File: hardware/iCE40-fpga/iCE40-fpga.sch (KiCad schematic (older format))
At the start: 45 parts, among them J1 USB_B_Micro, J2 JST_PH, J3 Feather, Q1 DMP2045U, U1 MCP73831-2-OT, U2 W25Q32JVZP, U3 AP2112K-3.3, U4 ICE40UP5K-SG48ITR, U5 NCV8114ASN120T1G, X1 DSC6101CI1A

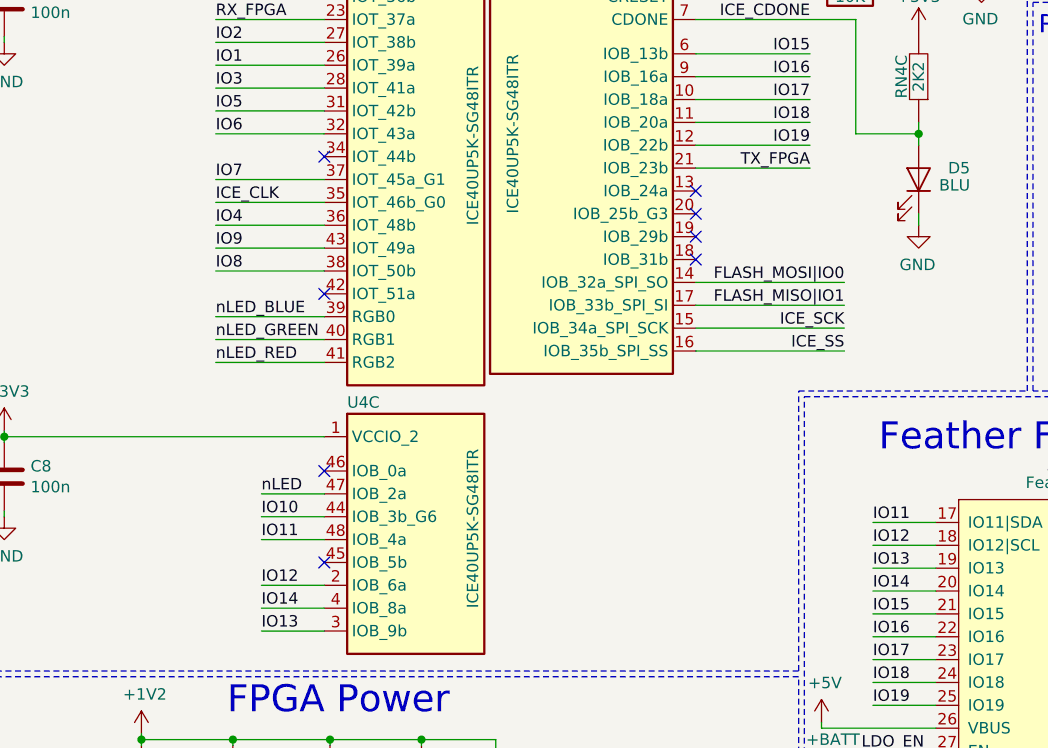
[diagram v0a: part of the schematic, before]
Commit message: broke out 4 pins to TP on bottom copper
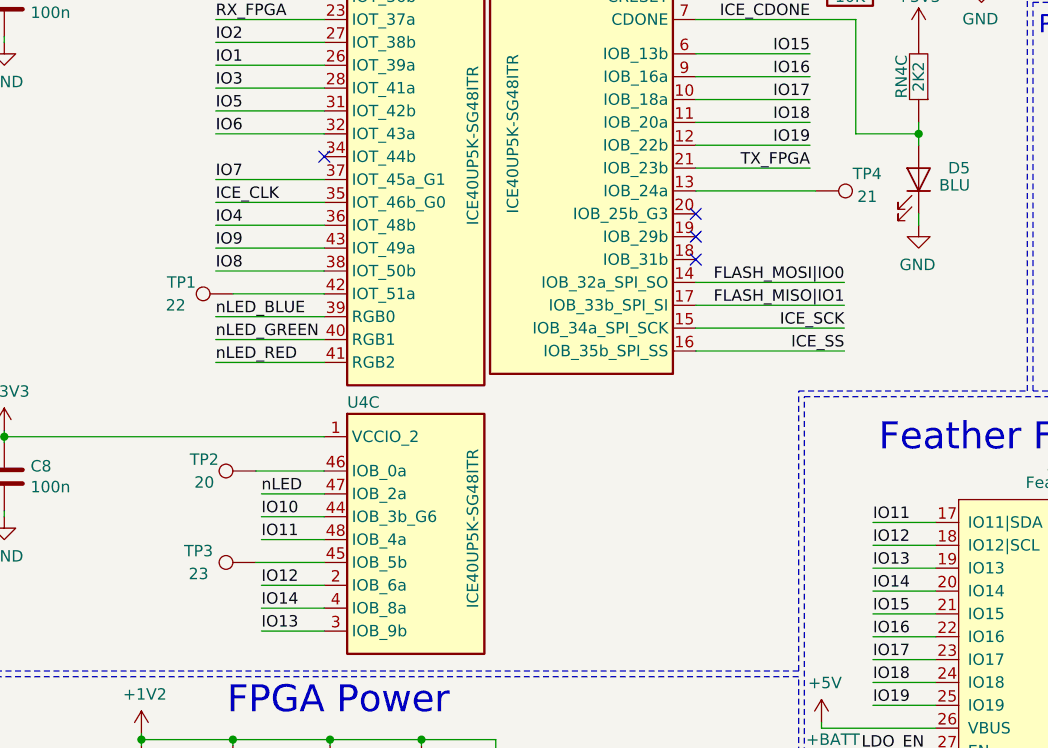
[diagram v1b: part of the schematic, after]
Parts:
- added TP1: 22, TestPoint:TestPoint_Pad_D1.5mm, symbol Connector:TestPoint
- added TP2: 20, TestPoint:TestPoint_Pad_D1.5mm, symbol Connector:TestPoint
- added TP3: 23, TestPoint:TestPoint_Pad_D1.5mm, symbol Connector:TestPoint
- added TP4: 21, TestPoint:TestPoint_Pad_D1.5mm, symbol Connector:TestPoint
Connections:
- net at U4.42 (IOT_51a): now also TP1.1
- net at U4.13 (IOB_24a): now also TP4.1
- net at U4.45 (IOB_5b): now also TP3.1
- net at U4.46 (IOB_0a): now also TP2.1
- no-connect marks 17 -> 13
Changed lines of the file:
@@
 	9875 5850 10000 5850
 NoConn ~ 6900 1900
-NoConn ~ 6900 2500
-NoConn ~ 8525 2350
 NoConn ~ 8525 2250
 NoConn ~ 8525 2150
-NoConn ~ 8525 2050
-NoConn ~ 6900 3275
+NoConn ~ 8525 2350
 Wire Wire Line
 	625  3100 975  3100
@@
 Wire Wire Line
 	10875 1975 10875 2025
-NoConn ~ 6900 3675
 Wire Wire Line
 	10700 1050 10725 1050
@@
 Wire Wire Line
 	4000 3300 4050 3300
+$Comp
+L Connector:TestPoint TP3
+U 1 1 5D23FA3D
+P 6600 3675
+F 0 "TP3" V 6650 3925 50  0000 C CNN
+F 1 "23" V 6550 3925 50  0000 C CNN
+F 2 "TestPoint:TestPoint_Pad_D1.5mm" H 6800 3675 50  0001 C CNN
+F 3 "~" H 6800 3675 50  0001 C CNN
+	1    6600 3675
+	0    -1   -1   0
+$EndComp
+Wire Wire Line
+	6600 3675 6900 3675
+$Comp
+L Connector:TestPoint TP2
+U 1 1 5D26AE62
+P 6600 3275
+F 0 "TP2" V 6650 3500 50  0000 C CNN
+F 1 "20" V 6550 3500 50  0000 C CNN
+F 2 "TestPoint:TestPoint_Pad_D1.5mm" H 6800 3275 50  0001 C CNN
+F 3 "~" H 6800 3275 50  0001 C CNN
+	1    6600 3275
+	0    -1   -1   0
+$EndComp
+Wire Wire Line
+	6600 3275 6900 3275
+$Comp
+L Connector:TestPoint TP1
+U 1 1 5D28130D
+P 6500 2500
+F 0 "TP1" V 6550 2725 50  0000 C CNN
+F 1 "22" V 6450 2750 50  0000 C CNN
+F 2 "TestPoint:TestPoint_Pad_D1.5mm" H 6700 2500 50  0001 C CNN
+F 3 "~" H 6700 2500 50  0001 C CNN
+	1    6500 2500
+	0    -1   -1   0
+$EndComp
+Wire Wire Line
+	6500 2500 6900 2500
+$Comp
+L Connector:TestPoint TP4
+U 1 1 5D2B0957
+P 9050 2050
+F 0 "TP4" V 8975 2275 50  0000 C CNN
+F 1 "21" V 9075 2275 50  0000 C CNN
+F 2 "TestPoint:TestPoint_Pad_D1.5mm" H 9250 2050 50  0001 C CNN
+F 3 "~" H 9250 2050 50  0001 C CNN
+	1    9050 2050
+	0    1    1    0
+$EndComp
+Wire Wire Line
+	9050 2050 8525 2050
 $EndSCHEMATC

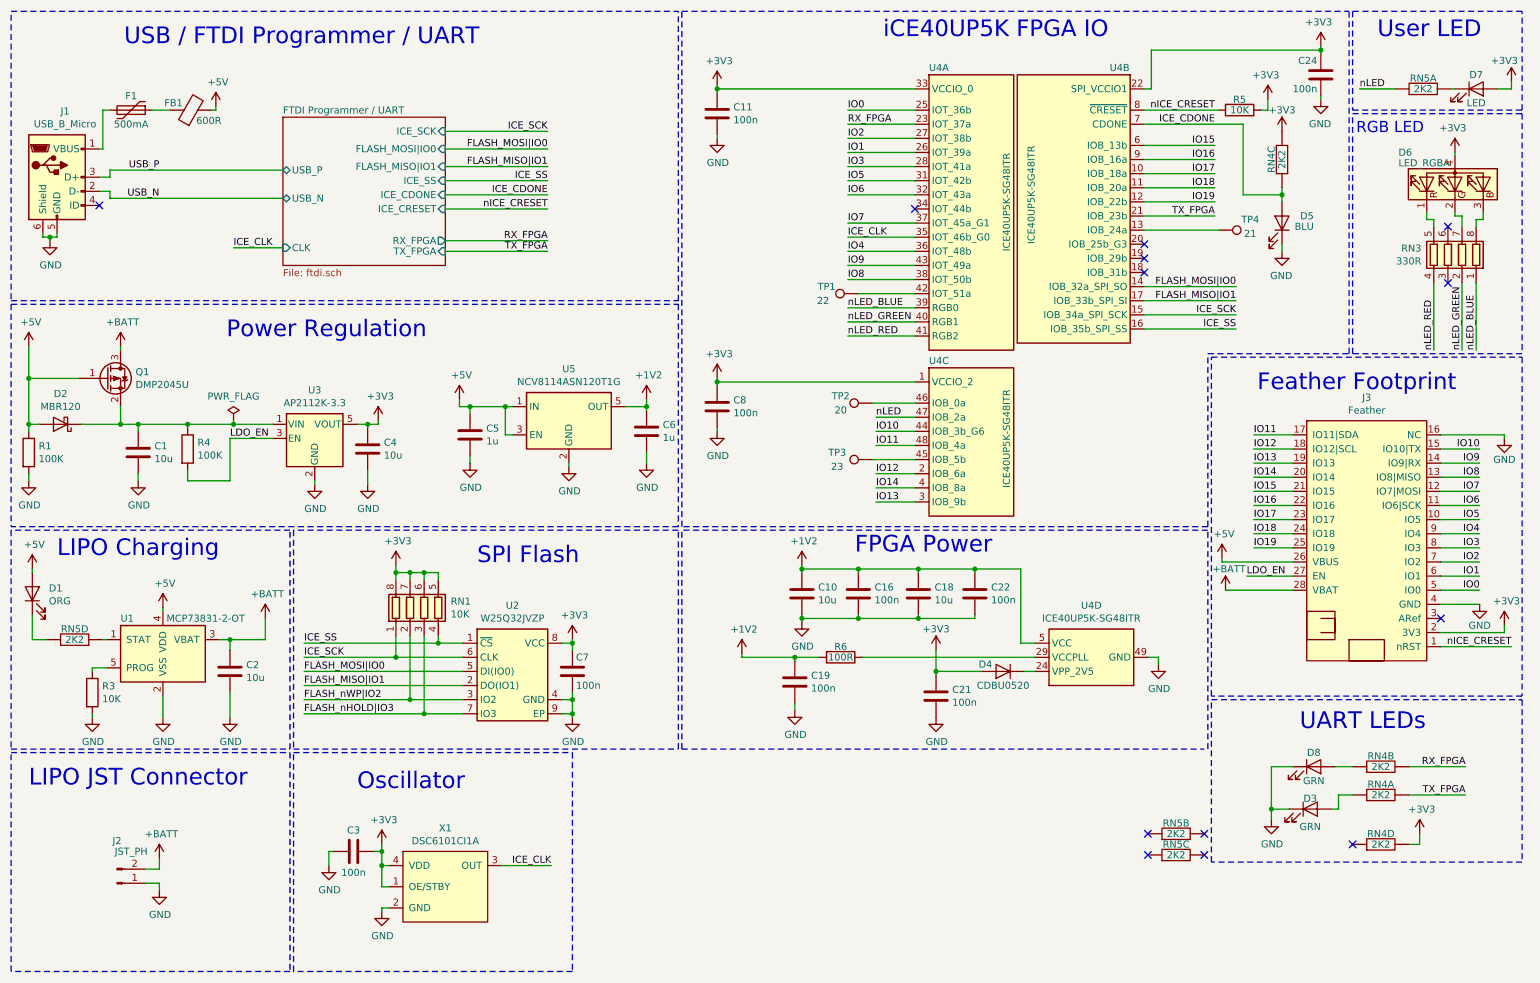
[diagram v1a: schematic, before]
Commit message: generated gerbers, changed pin labelling to match constraints file
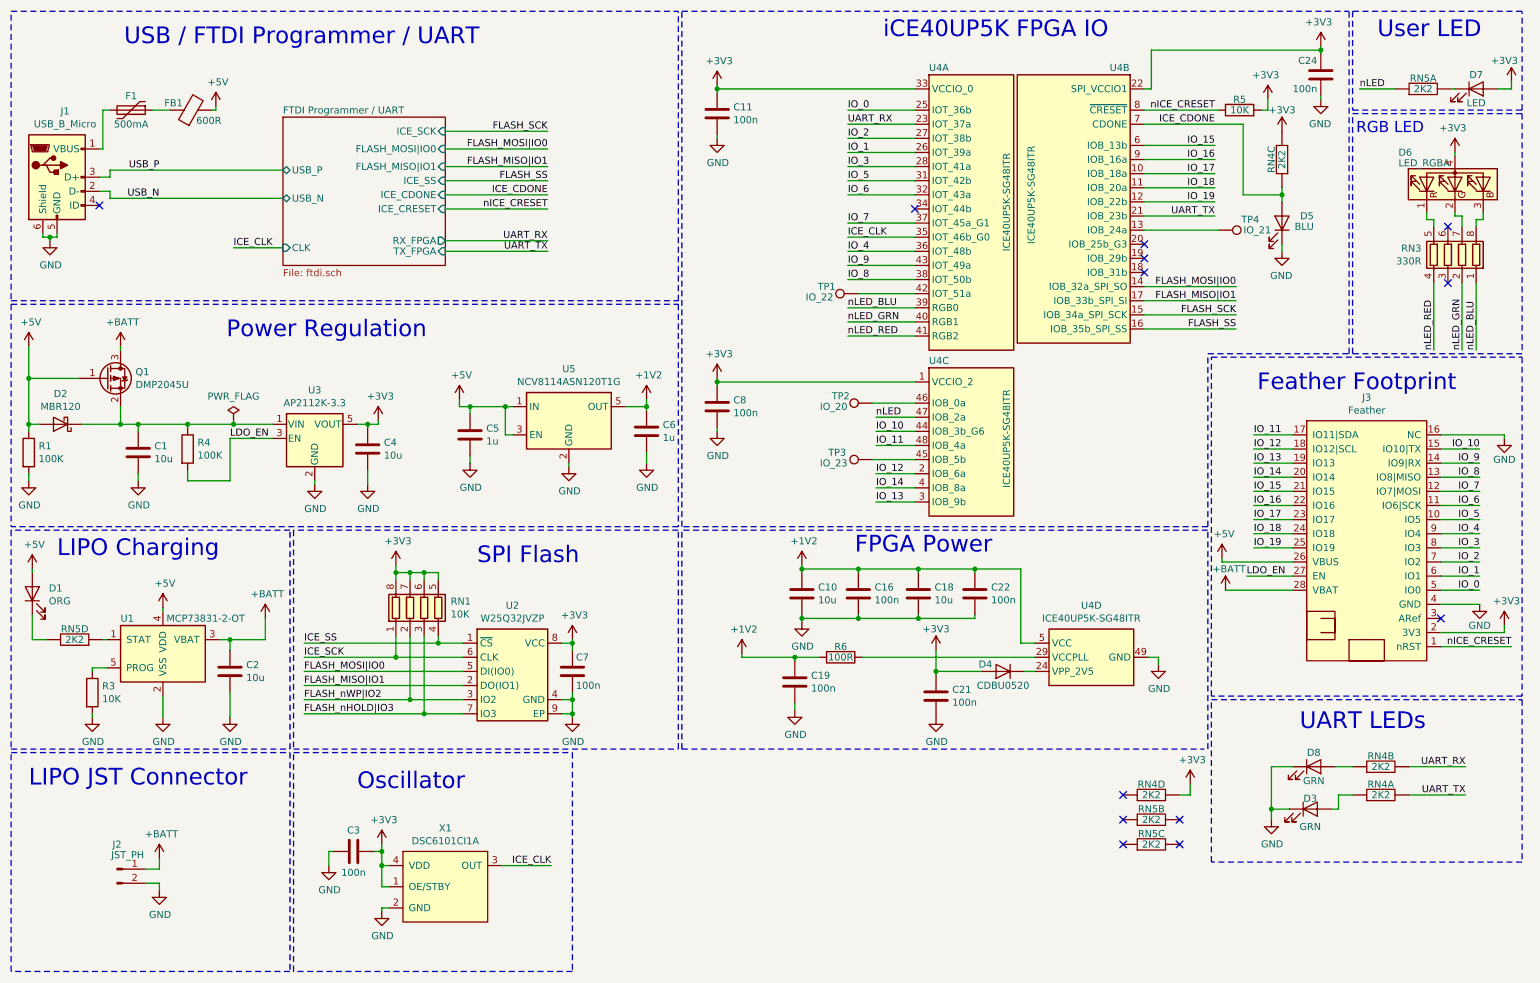
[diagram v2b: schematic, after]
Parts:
- TP1: value 22 -> IO_22
- TP2: value 20 -> IO_20
- TP3: value 23 -> IO_23
- TP4: value 21 -> IO_21
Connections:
- net +BATT: now also J2.1 (Pin_1); no longer J2.2 (Pin_2)
- net GND: now also J2.2 (Pin_2); no longer J2.1 (Pin_1)
- net ICE_SCK: no longer U4.15 (IOB_34a_SPI_SCK)
- net ICE_SS: no longer U4.16 (IOB_35b_SPI_SS)
- net IO0 renamed IO_0
- net IO1 renamed IO_1
- net IO10 renamed IO_10
- net IO11 renamed IO_11
- net IO12 renamed IO_12
- net IO13 renamed IO_13
- net IO14 renamed IO_14
- net IO15 renamed IO_15
- net IO16 renamed IO_16
- net IO17 renamed IO_17
- net IO18 renamed IO_18
- net IO19 renamed IO_19
- net IO2 renamed IO_2
- net IO3 renamed IO_3
- net IO4 renamed IO_4
- net IO5 renamed IO_5
- net IO6 renamed IO_6
- net IO7 renamed IO_7
- net IO8 renamed IO_8
- net IO9 renamed IO_9
- net RX_FPGA renamed UART_RX
- net TX_FPGA renamed UART_TX
- net nLED_BLUE renamed nLED_BLU
- net nLED_GREEN renamed nLED_GRN
- new net FLASH_SCK: U4.15 (IOB_34a_SPI_SCK)
- new net FLASH_SS: U4.16 (IOB_35b_SPI_SS)
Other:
- moved on the sheet: RN4D, RN5B, RN5C
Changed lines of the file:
@@
 Wire Wire Line
 	10875 2425 10875 2900
-Text Label 10875 2900 1    50   ~ 0
-nLED_BLUE
 Wire Wire Line
 	10775 2425 10775 2900
-Text Label 10775 2900 1    50   ~ 0
-nLED_GREEN
 Wire Wire Line
 	10575 2425 10575 2900
@@
 	6900 2600 6425 2600
 Text Label 6425 2600 0    50   ~ 0
-nLED_BLUE
+nLED_BLU
 Wire Wire Line
 	6900 2700 6425 2700
 Text Label 6425 2700 0    50   ~ 0
-nLED_GREEN
+nLED_GRN
 Wire Wire Line
 	6900 2800 6425 2800
@@
 	3575 1350 4300 1350
 Text Label 4300 1350 2    50   ~ 0
-ICE_SCK
+FLASH_SCK
 Wire Wire Line
 	3575 1475 4300 1475
@@
 	3575 1700 4300 1700
 Text Label 4300 1700 2    50   ~ 0
-ICE_SS
+FLASH_SS
 Wire Wire Line
 	3575 1800 4300 1800
@@
 ICE_CLK
 Text Label 4300 2200 2    50   ~ 0
-TX_FPGA
+UART_TX
 Text Label 4300 2125 2    50   ~ 0
-RX_FPGA
+UART_RX
 Text Label 9025 1950 2    50   ~ 0
-TX_FPGA
+UART_TX
 Text Label 6425 1300 0    50   ~ 0
-RX_FPGA
+UART_RX
 Wire Wire Line
 	8575 1050 8525 1050
@@
 Wire Wire Line
 	1450 6575 1550 6575
-$Comp
-L Connector:Conn_01x02_Male J2
-U 1 1 617F1813
-P 1250 6675
-F 0 "J2" H 1250 6375 50  0000 C CNN
-F 1 "JST_PH" H 1350 6450 50  0000 C CNN
-F 2 "josh-connectors:JST_PH_S2B-PH-SM4-TB_1x02-1MP_P2.00mm_Horizontal" H 1250 6675 50  0001 C CNN
-F 3 "~" H 1250 6675 50  0001 C CNN
-	1    1250 6675
-	1    0    0    1
-$EndComp
 Wire Wire Line
 	10725 1500 10725 1525
@@
 	8525 2650 9175 2650
 Text Label 9175 2650 2    50   ~ 0
-ICE_SCK
+FLASH_SCK
 Wire Wire Line
 	8525 2450 9175 2450
@@
 FLASH_MISO|IO1
 Text Label 9175 2750 2    50   ~ 0
-ICE_SS
+FLASH_SS
 Wire Wire Line
 	9175 2750 8525 2750
@@
 Wire Wire Line
 	9025 1950 8525 1950
-Text Label 10900 4600 2    50   ~ 0
-IO0
 Wire Wire Line
 	10900 4600 10625 4600
-Text Label 10900 4500 2    50   ~ 0
-IO1
 Wire Wire Line
 	10900 4500 10625 4500
-Text Label 10900 4400 2    50   ~ 0
-IO2
 Wire Wire Line
 	10900 4400 10625 4400
-Text Label 10900 4300 2    50   ~ 0
-IO3
 Wire Wire Line
 	10900 4300 10625 4300
-Text Label 6425 1200 0    50   ~ 0
-IO0
 Wire Wire Line
 	6425 1200 6900 1200
 Text Label 6425 1500 0    50   ~ 0
-IO1
+IO_1
 Wire Wire Line
 	6425 1500 6900 1500
 Text Label 6425 1400 0    50   ~ 0
-IO2
+IO_2
 Wire Wire Line
 	6425 1400 6900 1400
 Text Label 6425 1600 0    50   ~ 0
-IO3
+IO_3
 Wire Wire Line
 	6425 1600 6900 1600
-Text Label 10900 4200 2    50   ~ 0
-IO4
 Wire Wire Line
 	10900 4200 10625 4200
-Text Label 10900 4100 2    50   ~ 0
-IO5
 Wire Wire Line
 	10900 4100 10625 4100
 Text Label 6425 2200 0    50   ~ 0
-IO4
+IO_4
 Wire Wire Line
 	6425 2200 6900 2200
 Text Label 6425 1700 0    50   ~ 0
-IO5
+IO_5
 Wire Wire Line
 	6425 1700 6900 1700
 Text Label 6425 1800 0    50   ~ 0
-IO6
+IO_6
 Wire Wire Line
 	6425 1800 6900 1800
-Text Label 10900 4000 2    50   ~ 0
-IO6
 Wire Wire Line
 	10900 4000 10625 4000
-Text Label 9300 4300 0    50   ~ 0
-IO19
 Wire Wire Line
 	9300 4300 9575 4300
-Text Label 9300 4200 0    50   ~ 0
-IO18
 Wire Wire Line
 	9300 4200 9575 4200
-Text Label 9300 4100 0    50   ~ 0
-IO17
 Wire Wire Line
 	9300 4100 9575 4100
-Text Label 9300 4000 0    50   ~ 0
-IO16
 Wire Wire Line
 	9300 4000 9575 4000
-Text Label 9300 3900 0    50   ~ 0
-IO15
 Wire Wire Line
 	9300 3900 9575 3900
-Text Label 9300 3800 0    50   ~ 0
-IO14
 Wire Wire Line
 	9300 3800 9575 3800
-Text Label 9300 3700 0    50   ~ 0
-IO13
 Wire Wire Line
 	9300 3700 9575 3700
-Text Label 9300 3600 0    50   ~ 0
-IO12
 Wire Wire Line
 	9300 3600 9575 3600
-Text Label 9300 3500 0    50   ~ 0
-IO11
 Wire Wire Line
 	9300 3500 9575 3500
-Text Label 10900 3800 2    50   ~ 0
-IO8
 Wire Wire Line
 	10900 3800 10625 3800
-Text Label 10900 3700 2    50   ~ 0
-IO9
 Wire Wire Line
 	10900 3700 10625 3700
 Text Label 9025 1850 2    50   ~ 0
-IO19
+IO_19
 Wire Wire Line
 	9025 1850 8525 1850
 Text Label 9025 1750 2    50   ~ 0
-IO18
+IO_18
 Wire Wire Line
 	9025 1750 8525 1750
 Text Label 9025 1650 2    50   ~ 0
-IO17
+IO_17
 Wire Wire Line
 	9025 1650 8525 1650
 Text Label 9025 1550 2    50   ~ 0
-IO16
+IO_16
 Wire Wire Line
 	9025 1550 8525 1550
 Text Label 9025 1450 2    50   ~ 0
-IO15
+IO_15
 Wire Wire Line
 	9025 1450 8525 1450
 Text Label 6625 3875 0    50   ~ 0
-IO14
+IO_14
 Wire Wire Line
 	6625 3875 6900 3875
 Text Label 6625 3975 0    50   ~ 0
-IO13
+IO_13
 Wire Wire Line
 	6625 3975 6900 3975
 Text Label 6625 3775 0    50   ~ 0
-IO12
+IO_12
 Wire Wire Line
 	6625 3775 6900 3775
 Text Label 6625 3575 0    50   ~ 0
-IO11
+IO_11
 Wire Wire Line
 	6625 3575 6900 3575
 Text Label 6425 2400 0    50   ~ 0
-IO8
+IO_8
 Text Label 6425 2300 0    50   ~ 0
-IO9
+IO_9
 Wire Wire Line
 	6425 2300 6900 2300
@@
 Wire Wire Line
 	10900 3600 10625 3600
-Text Label 10900 3600 2    50   ~ 0
-IO10
 Wire Wire Line
 	10900 3900 10625 3900
-Text Label 10900 3900 2    50   ~ 0
-IO7
 Wire Wire Line
 	6625 3475 6900 3475
 Text Label 6625 3475 0    50   ~ 0
-IO10
+IO_10
 Wire Wire Line
 	6425 2000 6900 2000
 Text Label 6425 2000 0    50   ~ 0
-IO7
+IO_7
 $Comp
 L Device:LED D8
@@
 	1    0    0    -1
 $EndComp
-Text Label 10800 6050 2    50   ~ 0
-TX_FPGA
-Text Label 10800 5850 2    50   ~ 0
-RX_FPGA
 Wire Wire Line
 	9575 5850 9425 5850
@@
 L josh-passive:RN RN4
 U 4 1 5D4398FC
-P 10200 6400
-F 0 "RN4" H 10200 6475 50  0000 C CNN
-F 1 "2K2" H 10200 6400 50  0000 C CNN
-F 2 "Resistor_SMD:R_Array_Convex_4x0402" V 10200 6400 50  0001 C CNN
-F 3 "~" V 10200 6400 50  0001 C CNN
-	4    10200 6400
+P 8575 6050
+F 0 "RN4" H 8575 6125 50  0000 C CNN
+F 1 "2K2" H 8575 6050 50  0000 C CNN
+F 2 "Resistor_SMD:R_Array_Convex_4x0402" V 8575 6050 50  0001 C CNN
+F 3 "~" V 8575 6050 50  0001 C CNN
+	4    8575 6050
 	1    0    0    -1
 $EndComp
@@
 L power:+3V3 #PWR0108
 U 1 1 5D85EEC4
-P 10475 6325
-F 0 "#PWR0108" H 10475 6175 50  0001 C CNN
-F 1 "+3V3" H 10490 6498 50  0000 C CNN
-F 2 "" H 10475 6325 50  0001 C CNN
-F 3 "" H 10475 6325 50  0001 C CNN
-	1    10475 6325
-	1    0    0    -1
-$EndComp
-Wire Wire Line
-	10475 6325 10475 6400
-Wire Wire Line
-	10475 6400 10400 6400
-NoConn ~ 10000 6400
+P 8850 5975
+F 0 "#PWR0108" H 8850 5825 50  0001 C CNN
+F 1 "+3V3" H 8865 6148 50  0000 C CNN
+F 2 "" H 8850 5975 50  0001 C CNN
+F 3 "" H 8850 5975 50  0001 C CNN
+	1    8850 5975
+	1    0    0    -1
+$EndComp
+Wire Wire Line
+	8850 5975 8850 6050
+Wire Wire Line
+	8850 6050 8775 6050
+NoConn ~ 8375 6050
 Wire Wire Line
 	10525 1925 10525 1975
@@
 L josh-passive:RN RN5
 U 2 1 5D221617
-P 8750 6325
-F 0 "RN5" H 8750 6400 50  0000 C CNN
-F 1 "2K2" H 8750 6325 50  0000 C CNN
-F 2 "Resistor_SMD:R_Array_Convex_4x0402" V 8750 6325 50  0001 C CNN
-F 3 "~" V 8750 6325 50  0001 C CNN
-	2    8750 6325
+P 8575 6225
+F 0 "RN5" H 8575 6300 50  0000 C CNN
+F 1 "2K2" H 8575 6225 50  0000 C CNN
+F 2 "Resistor_SMD:R_Array_Convex_4x0402" V 8575 6225 50  0001 C CNN
+F 3 "~" V 8575 6225 50  0001 C CNN
+	2    8575 6225
 	1    0    0    -1
 $EndComp
@@
 L josh-passive:RN RN5
 U 3 1 5D220693
-P 8750 6475
-F 0 "RN5" H 8750 6550 50  0000 C CNN
-F 1 "2K2" H 8750 6475 50  0000 C CNN
-F 2 "Resistor_SMD:R_Array_Convex_4x0402" V 8750 6475 50  0001 C CNN
-F 3 "~" V 8750 6475 50  0001 C CNN
-	3    8750 6475
+P 8575 6400
+F 0 "RN5" H 8575 6475 50  0000 C CNN
+F 1 "2K2" H 8575 6400 50  0000 C CNN
+F 2 "Resistor_SMD:R_Array_Convex_4x0402" V 8575 6400 50  0001 C CNN
+F 3 "~" V 8575 6400 50  0001 C CNN
+	3    8575 6400
 	1    0    0    -1
 $EndComp
@@
 	-1   0    0    -1
 $EndComp
-NoConn ~ 8950 6325
-NoConn ~ 8950 6475
-NoConn ~ 8550 6475
-NoConn ~ 8550 6325
+NoConn ~ 8775 6225
+NoConn ~ 8775 6400
+NoConn ~ 8375 6400
+NoConn ~ 8375 6225
 Text Label 2050 3525 0    50   ~ 0
 LDO_EN
@@
 P 6600 3675
 F 0 "TP3" V 6650 3925 50  0000 C CNN
-F 1 "23" V 6550 3925 50  0000 C CNN
+F 1 "IO_23" V 6575 3950 50  0000 C CNN
 F 2 "TestPoint:TestPoint_Pad_D1.5mm" H 6800 3675 50  0001 C CNN
 F 3 "~" H 6800 3675 50  0001 C CNN
@@
 P 6600 3275
 F 0 "TP2" V 6650 3500 50  0000 C CNN
-F 1 "20" V 6550 3500 50  0000 C CNN
+F 1 "IO_20" V 6575 3550 50  0000 C CNN
 F 2 "TestPoint:TestPoint_Pad_D1.5mm" H 6800 3275 50  0001 C CNN
 F 3 "~" H 6800 3275 50  0001 C CNN
@@
 P 6500 2500
 F 0 "TP1" V 6550 2725 50  0000 C CNN
-F 1 "22" V 6450 2750 50  0000 C CNN
+F 1 "IO_22" V 6475 2775 50  0000 C CNN
 F 2 "TestPoint:TestPoint_Pad_D1.5mm" H 6700 2500 50  0001 C CNN
 F 3 "~" H 6700 2500 50  0001 C CNN
@@
 P 9050 2050
 F 0 "TP4" V 8975 2275 50  0000 C CNN
-F 1 "21" V 9075 2275 50  0000 C CNN
+F 1 "IO_21" V 9050 2325 50  0000 C CNN
 F 2 "TestPoint:TestPoint_Pad_D1.5mm" H 9250 2050 50  0001 C CNN
 F 3 "~" H 9250 2050 50  0001 C CNN
@@
 Wire Wire Line
 	9050 2050 8525 2050
+$Comp
+L Connector:Conn_01x02_Male J2
+U 1 1 5D367D4D
+P 1250 6575
+F 0 "J2" H 1250 6750 50  0000 C CNN
+F 1 "JST_PH" H 1325 6675 50  0000 C CNN
+F 2 "josh-connectors:JST_PH_S2B-PH-SM4-TB_1x02-1MP_P2.00mm_Horizontal" H 1250 6575 50  0001 C CNN
+F 3 "~" H 1250 6575 50  0001 C CNN
+	1    1250 6575
+	1    0    0    -1
+$EndComp
+Text Label 10800 5850 2    50   ~ 0
+UART_RX
+Text Label 10800 6050 2    50   ~ 0
+UART_TX
+Text Label 10775 2900 1    50   ~ 0
+nLED_GRN
+Text Label 10875 2900 1    50   ~ 0
+nLED_BLU
+Text Label 6425 1200 0    50   ~ 0
+IO_0
+Text Label 10900 4600 2    50   ~ 0
+IO_0
+Text Label 10900 4500 2    50   ~ 0
+IO_1
+Text Label 10900 4400 2    50   ~ 0
+IO_2
+Text Label 10900 4300 2    50   ~ 0
+IO_3
+Text Label 10900 4200 2    50   ~ 0
+IO_4
+Text Label 10900 4100 2    50   ~ 0
+IO_5
+Text Label 10900 4000 2    50   ~ 0
+IO_6
+Text Label 10900 3900 2    50   ~ 0
+IO_7
+Text Label 10900 3800 2    50   ~ 0
+IO_8
+Text Label 10900 3700 2    50   ~ 0
+IO_9
+Text Label 10900 3600 2    50   ~ 0
+IO_10
+Text Label 9300 3500 0    50   ~ 0
+IO_11
+Text Label 9300 3600 0    50   ~ 0
+IO_12
+Text Label 9300 3800 0    50   ~ 0
+IO_14
+Text Label 9300 3700 0    50   ~ 0
+IO_13
+Text Label 9300 3900 0    50   ~ 0
+IO_15
+Text Label 9300 4000 0    50   ~ 0
+IO_16
+Text Label 9300 4100 0    50   ~ 0
+IO_17
+Text Label 9300 4200 0    50   ~ 0
+IO_18
+Text Label 9300 4300 0    50   ~ 0
+IO_19
 $EndSCHEMATC
